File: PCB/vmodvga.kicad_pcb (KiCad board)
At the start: 2 copper layers, 80 x 60.1 mm, 68 parts, among them J1 DE-15, J2 DE-15, J3 VHDCI, P1 50R, P2 50R, P3 50R, P4 50R, U1 ADP3303-3V3, U2 ADP3334, U3 AD9984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

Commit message: Two Layer Design Complete
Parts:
- added P5: CONN_1, PIN_ARRAY_1, F.Cu at (98.6, 106.2)
- added P6: CONN_1, PIN_ARRAY_1, F.Cu at (98.8, 100.3)
- C15, C16, Cp1, Cp2, Cp3, Cp4, Cp5, Cp6, FB4, FB5, FB6, R10, R13, R14, R17, R18, R8, R9, U1, U2, U4: moved to B.Cu
- C17, C18, C19, C2, C21, C22, C23, C24, C25, C3, C4, C5: footprint SM0805 -> SM0603; moved to B.Cu
- moved J1 50.3 mm to (149.5, 105.3), turned to 0 degrees
- moved Cp4 50.2 mm to (129.4, 56.0), turned to 90 degrees
- moved U4 48.1 mm to (137.5, 55.5), turned to 90 degrees
- moved R17 46.5 mm to (139.4, 51.7)
- moved Cp6 42.4 mm to (147.8, 55.6), turned to 270 degrees
- moved FB3 34.6 mm to (144.9, 96.6), turned to 90 degrees
- moved FB2 33.5 mm to (147.1, 96.6), turned to 90 degrees
- moved C22 33.3 mm to (135.5, 63.2)
- moved C23 33.3 mm to (135.5, 61.3)
- moved C21 33.3 mm to (135.5, 65.1)
- moved FB1 33.0 mm to (149.4, 96.6), turned to 90 degrees
- moved C24 31.1 mm to (139.8, 61.8)
- moved C25 31.1 mm to (139.8, 63.6)
- moved R18 31.1 mm to (139.8, 65.4)
- moved R12 11.3 mm to (121.0, 83.5)
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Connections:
- J3 pad 1: /R0 -> /VSOUT
- J3 pad 10: /VSOUT -> /R5
- J3 pad 12: /G9 -> /R3
- J3 pad 13: /G7 -> /R2
- J3 pad 15: /DATACK -> /R1
- J3 pad 20: /G5 -> /R0
- J3 pad 23: /G1 -> /G2
- J3 pad 26: /B7 -> /B8
- J3 pad 29: /B3 -> /B4
- J3 pad 3: /R2 -> /HSOUT
- J3 pad 31: /B2 -> /B1
- J3 pad 34: /CLAMP -> /SDA
- J3 pad 35: /R1 -> /OE_Field
- J3 pad 37: /R3 -> /PWRDWN
- J3 pad 38: /R5 -> /R9
- J3 pad 4: /R4 -> /SOGOUT
- J3 pad 40: /R7 -> /G9
- J3 pad 41: /R9 -> /G8
- J3 pad 43: /HSOUT -> /G7
- J3 pad 44: /G8 -> /R4
- J3 pad 45: /OE_Field -> /GND
- J3 pad 46: (no net) -> /G6
- J3 pad 47: /G6 -> /G5
- J3 pad 49: /G4 -> /DATACK
- J3 pad 54: /G2 -> /G4
- J3 pad 56: /G0 -> /G1
- J3 pad 57: /B8 -> /G0
- J3 pad 6: /R6 -> /R8
- J3 pad 60: (no net) -> /B7
- J3 pad 62: (no net) -> /B3
- J3 pad 63: /B4 -> /B2
- J3 pad 65: /SCL -> /CLAMP
- J3 pad 66: /B1 -> /COST
- J3 pad 68: /SDA -> /SCL
- J3 pad 7: /R8 -> /R7
- J3 pad 9: /SOGOUT -> /R6
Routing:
- net /PWRDWN: track 8.61 -> 69.3 mm
- net /HSOUT: track 0.00 -> 43.8 mm
- net /R9: track 0.00 -> 42.4 mm
- net /SOGOUT: track 0.00 -> 41.3 mm
- net /DATACK: track 0.00 -> 40.6 mm, vias 0 -> 1
- net /R8: track 0.00 -> 38.4 mm
- net /R7: track 0.00 -> 38.4 mm
- net /GND: track 175.7 -> 138.2 mm, vias 22 -> 16
- net /R6: track 0.00 -> 35.8 mm
- net /R4: track 0.00 -> 35.3 mm
- net /R5: track 0.00 -> 33.6 mm
- net /VSOUT: track 14.0 -> 47.6 mm, vias 2 -> 1
- net /R3: track 0.00 -> 31.2 mm
- net /R2: track 0.00 -> 31.1 mm
- net /CLAMP: track 12.3 -> 42.9 mm
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
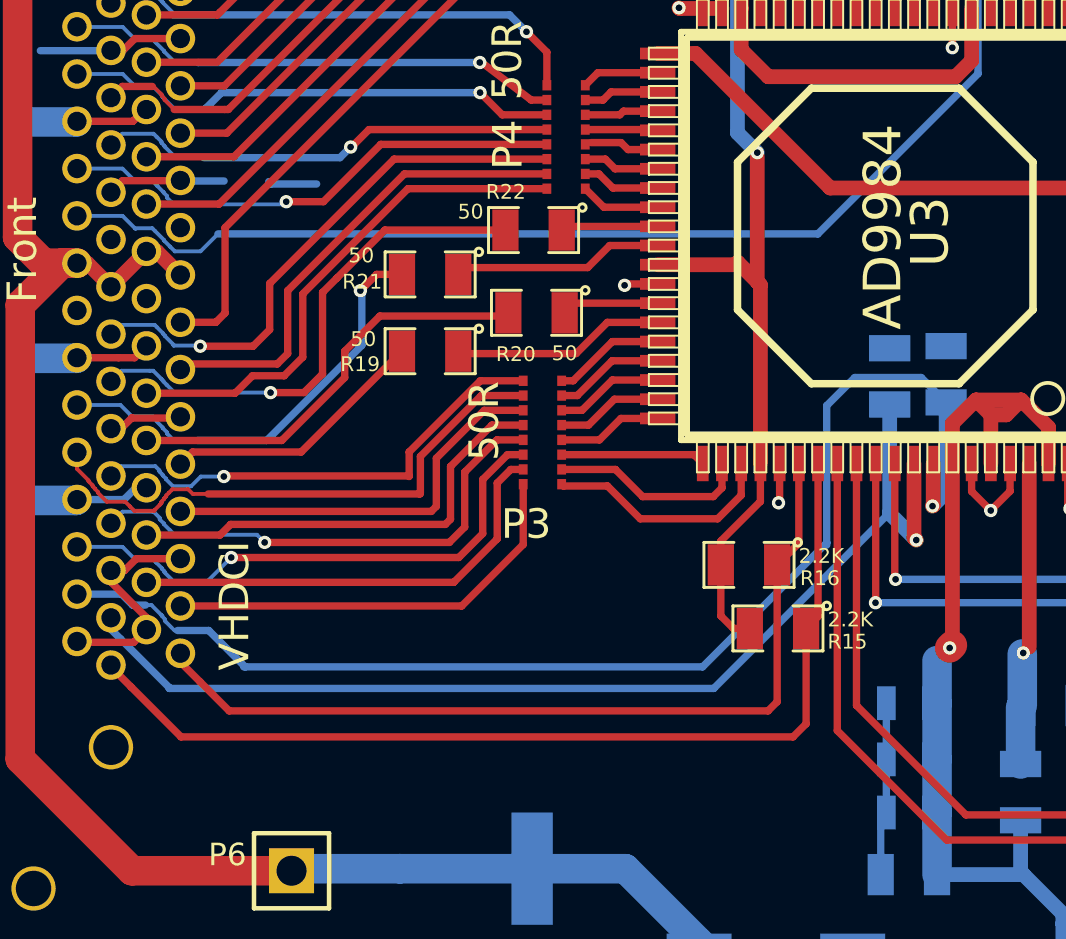
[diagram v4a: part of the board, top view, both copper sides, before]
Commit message: Some labels moved to proper location
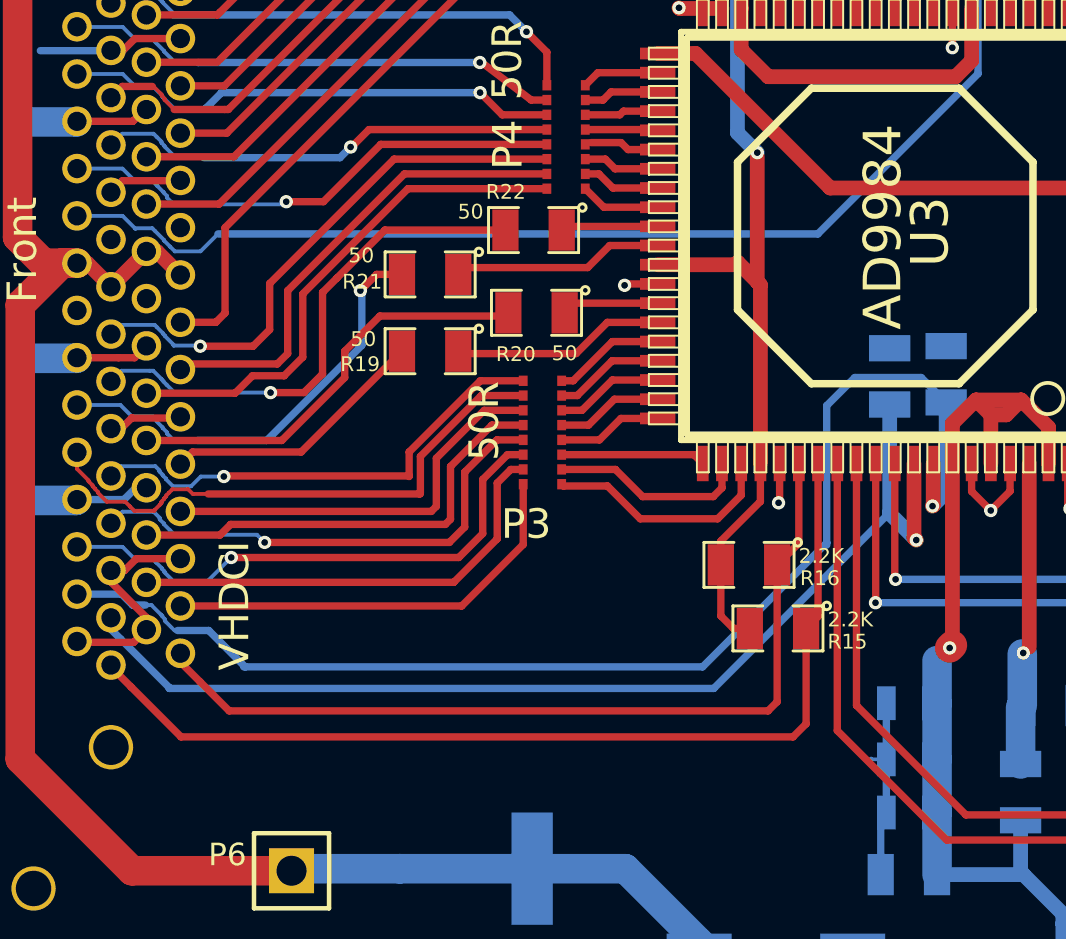
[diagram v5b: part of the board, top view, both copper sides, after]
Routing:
- net /GND: track 138.2 -> 135.6 mm
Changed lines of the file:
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@@
   (general
     (links 253)
-    (no_connects 2)
+    (no_connects 3)
     (area 46.3975 49.249999 167.950001 168.4525)
     (thickness 1.6)
     (drawings 7)
-    (tracks 1064)
+    (tracks 1063)
     (zones 0)
     (modules 70)
@@
   )
   (setup
-    (last_trace_width 0.25)
+    (last_trace_width 0.125)
     (user_trace_width 0.13)
     (user_trace_width 0.25)
@@
     (at 121.1 104.61 270)
     (attr smd)
-    (fp_text reference R13 (at 0 0.3175 270) (layer B.SilkS)
+    (fp_text reference R13 (at 2.9 0.23 360) (layer B.SilkS)
       (effects (font (size 0.50038 0.50038) (thickness 0.10922)) (justify mirror))
     )
-    (fp_text value 76.8k (at 0 -0.381 270) (layer B.SilkS)
+    (fp_text value 76.8k (at 2.23 -0.08 360) (layer B.SilkS)
       (effects (font (size 0.50038 0.50038) (thickness 0.10922)) (justify mirror))
     )
@@
     (at 107.62 59.56 180)
     (attr smd)
-    (fp_text reference C2 (at 0 0 180) (layer B.SilkS)
+    (fp_text reference C2 (at 1.73 0.34 180) (layer B.SilkS)
       (effects (font (size 0.508 0.4572) (thickness 0.1143)) (justify mirror))
     )
-    (fp_text value .1uf (at 0 0 180) (layer B.SilkS) hide
+    (fp_text value .1uf (at 1.89 -0.36 180) (layer B.SilkS) hide
       (effects (font (size 0.508 0.4572) (thickness 0.1143)) (justify mirror))
     )
@@
     (at 107.62 61.56 180)
     (attr smd)
-    (fp_text reference C3 (at 0 0 180) (layer B.SilkS)
+    (fp_text reference C3 (at 1.7 0.47 180) (layer B.SilkS)
       (effects (font (size 0.508 0.4572) (thickness 0.1143)) (justify mirror))
     )
-    (fp_text value .1uf (at 0 0 180) (layer B.SilkS) hide
+    (fp_text value .1uf (at 1.88 -0.29 180) (layer B.SilkS) hide
       (effects (font (size 0.508 0.4572) (thickness 0.1143)) (justify mirror))
     )
@@
     (at 107.63 63.82 180)
     (attr smd)
-    (fp_text reference C4 (at 0 0 180) (layer B.SilkS)
+    (fp_text reference C4 (at 1.85 -0.39 180) (layer B.SilkS)
       (effects (font (size 0.508 0.4572) (thickness 0.1143)) (justify mirror))
     )
-    (fp_text value .1uf (at 0 0 180) (layer B.SilkS) hide
+    (fp_text value .1uf (at 1.84 0.45 180) (layer B.SilkS) hide
       (effects (font (size 0.508 0.4572) (thickness 0.1143)) (justify mirror))
     )
@@
     (at 112.74 61.49 90)
     (attr smd)
-    (fp_text reference C5 (at 0 0 90) (layer B.SilkS)
+    (fp_text reference C5 (at 0.75 1.14 90) (layer B.SilkS)
       (effects (font (size 0.508 0.4572) (thickness 0.1143)) (justify mirror))
     )
-    (fp_text value .1uf (at 0 0 90) (layer B.SilkS) hide
+    (fp_text value .1uf (at -0.48 1.24 90) (layer B.SilkS) hide
       (effects (font (size 0.508 0.4572) (thickness 0.1143)) (justify mirror))
     )
@@
     (at 135.525 65.055 180)
     (attr smd)
-    (fp_text reference C21 (at 0 0 180) (layer B.SilkS)
+    (fp_text reference C21 (at 2.045 0.315 180) (layer B.SilkS)
       (effects (font (size 0.508 0.4572) (thickness 0.1143)) (justify mirror))
     )
-    (fp_text value .1uf (at 0 0 180) (layer B.SilkS) hide
+    (fp_text value .1uf (at 1.995 -0.455 180) (layer B.SilkS) hide
       (effects (font (size 0.508 0.4572) (thickness 0.1143)) (justify mirror))
     )
@@
     (at 135.525 63.155 180)
     (attr smd)
-    (fp_text reference C22 (at 0 0 180) (layer B.SilkS)
+    (fp_text reference C22 (at 2.075 0.395 180) (layer B.SilkS)
       (effects (font (size 0.508 0.4572) (thickness 0.1143)) (justify mirror))
     )
-    (fp_text value .1uf (at 0 0 180) (layer B.SilkS) hide
+    (fp_text value .1uf (at 1.945 -0.345 180) (layer B.SilkS) hide
       (effects (font (size 0.508 0.4572) (thickness 0.1143)) (justify mirror))
     )
@@
     (at 135.525 61.255 180)
     (attr smd)
-    (fp_text reference C23 (at 0 0 180) (layer B.SilkS)
+    (fp_text reference C23 (at 2.075 0.495 180) (layer B.SilkS)
       (effects (font (size 0.508 0.4572) (thickness 0.1143)) (justify mirror))
     )
-    (fp_text value .1uf (at 0 0 180) (layer B.SilkS) hide
+    (fp_text value .1uf (at 1.845 -0.235 180) (layer B.SilkS) hide
       (effects (font (size 0.508 0.4572) (thickness 0.1143)) (justify mirror))
     )
@@
     (at 139.805 61.815)
     (attr smd)
-    (fp_text reference C24 (at 0 0) (layer B.SilkS)
+    (fp_text reference C24 (at 1.955 -0.475) (layer B.SilkS)
       (effects (font (size 0.508 0.4572) (thickness 0.1143)) (justify mirror))
     )
-    (fp_text value .1uf (at 0 0) (layer B.SilkS) hide
+    (fp_text value .1uf (at 2.005 0.235) (layer B.SilkS) hide
       (effects (font (size 0.508 0.4572) (thickness 0.1143)) (justify mirror))
     )
@@
     (at 139.805 63.615)
     (attr smd)
-    (fp_text reference C25 (at 0 0) (layer B.SilkS)
+    (fp_text reference C25 (at 2.105 -0.345) (layer B.SilkS)
       (effects (font (size 0.508 0.4572) (thickness 0.1143)) (justify mirror))
     )
-    (fp_text value .1uf (at 0 0) (layer B.SilkS) hide
+    (fp_text value .1uf (at 2.135 0.295) (layer B.SilkS) hide
       (effects (font (size 0.508 0.4572) (thickness 0.1143)) (justify mirror))
     )
@@
     (at 119.7 98.31 180)
     (attr smd)
-    (fp_text reference C17 (at 0 0 180) (layer B.SilkS)
+    (fp_text reference C17 (at 2.3 0.63 180) (layer B.SilkS)
       (effects (font (size 0.508 0.4572) (thickness 0.1143)) (justify mirror))
     )
-    (fp_text value .1uf (at 0 0 180) (layer B.SilkS) hide
+    (fp_text value .1uf (at 2.05 -0.21 180) (layer B.SilkS) hide
       (effects (font (size 0.508 0.4572) (thickness 0.1143)) (justify mirror))
     )
@@
     (at 119.7 94.61 180)
     (attr smd)
-    (fp_text reference C19 (at 0 0 180) (layer B.SilkS)
+    (fp_text reference C19 (at 2.01 0.39 180) (layer B.SilkS)
       (effects (font (size 0.508 0.4572) (thickness 0.1143)) (justify mirror))
     )
-    (fp_text value .1uf (at 0 0 180) (layer B.SilkS) hide
+    (fp_text value .1uf (at 1.96 -0.27 180) (layer B.SilkS) hide
       (effects (font (size 0.508 0.4572) (thickness 0.1143)) (justify mirror))
     )
@@
     (at 119.7 96.51 180)
     (attr smd)
-    (fp_text reference C18 (at 0 0 180) (layer B.SilkS)
+    (fp_text reference C18 (at 1.99 0.48 180) (layer B.SilkS)
       (effects (font (size 0.508 0.4572) (thickness 0.1143)) (justify mirror))
     )
-    (fp_text value .1uf (at 0 0 180) (layer B.SilkS) hide
+    (fp_text value .1uf (at 1.85 -0.31 180) (layer B.SilkS) hide
       (effects (font (size 0.508 0.4572) (thickness 0.1143)) (justify mirror))
     )
@@
   (segment (start 94.27 70.71) (end 94.12 70.56) (width 0.13) (layer B.Cu) (net 23))
   (segment (start 92.97 70.92) (end 92.7 70.92) (width 0.13) (layer B.Cu) (net 23) (status 30))
-  (segment (start 98.04 76.96) (end 98.12 77.04) (width 0.25) (layer B.Cu) (net 24))
-  (segment (start 98.12 77.04) (end 99.66 77.04) (width 0.25) (layer B.Cu) (net 24))
-  (segment (start 95.05 76.92) (end 95.07 76.94) (width 0.25) (layer B.Cu) (net 24) (status C00000))
-  (segment (start 95.07 76.94) (end 96.53 76.94) (width 0.25) (layer B.Cu) (net 24) (status 400000))
+  (segment (start 118.938 96.51) (end 118.45 96.51) (width 0.125) (layer B.Cu) (net 24) (status 400000))
+  (segment (start 118.45 96.51) (end 118.42 96.48) (width 0.125) (layer B.Cu) (net 24))
+  (segment (start 95.05 76.92) (end 95.07 76.94) (width 0.25) (layer B.Cu) (net 24))
   (segment (start 92.69 72.53) (end 90.31 72.53) (width 0.25) (layer B.Cu) (net 24))
   (segment (start 92.7 72.52) (end 92.69 72.53) (width 0.25) (layer B.Cu) (net 24))

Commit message: some updates and pdf generated
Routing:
- net /HSYNC0: track 69.0 -> 62.1 mm
- net /GND: track 135.6 -> 138.1 mm
- net /OVDD: track 79.5 -> 80.3 mm
